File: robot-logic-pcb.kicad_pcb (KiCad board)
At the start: 2 copper layers, 101.6 x 53.3 mm, 21 parts, among them U1 NRF24L01_Breakout

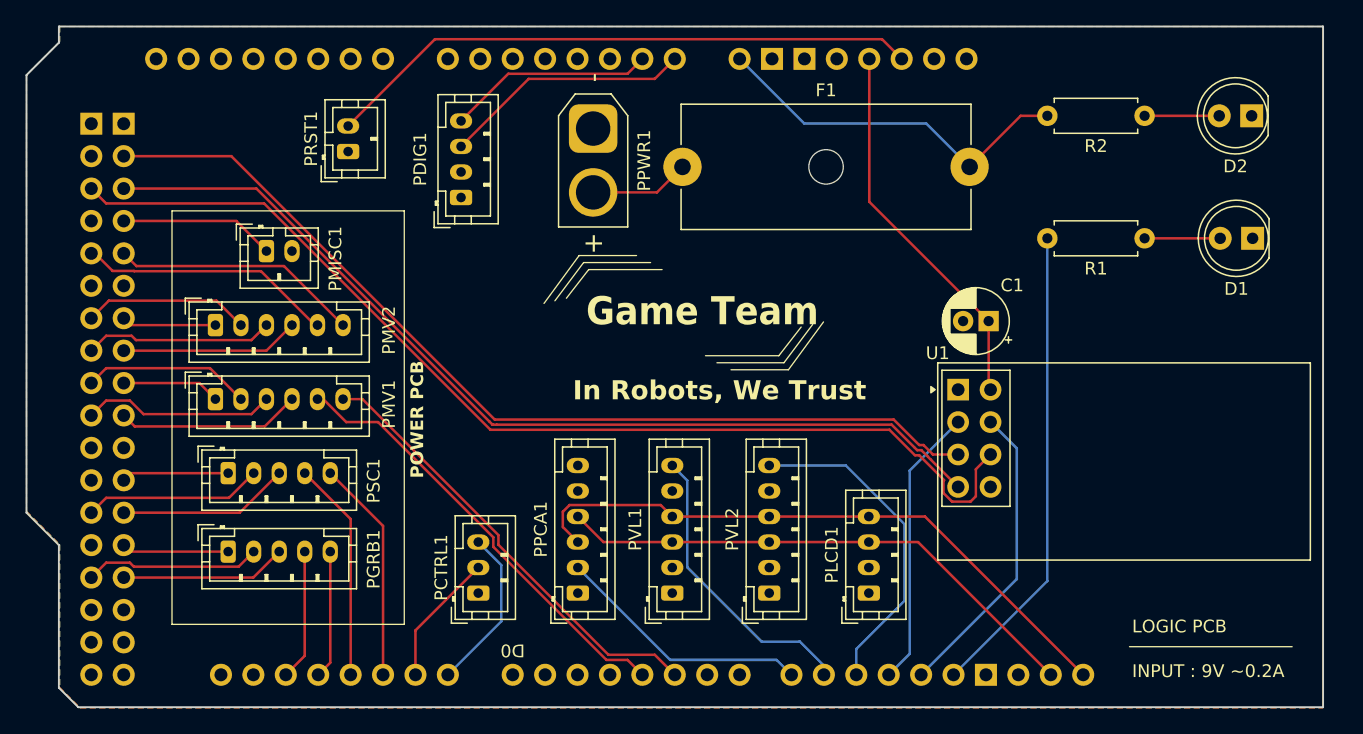
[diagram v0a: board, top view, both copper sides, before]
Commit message: Post regionales Adds ESP32 for steppers and diodes to protect MCUs
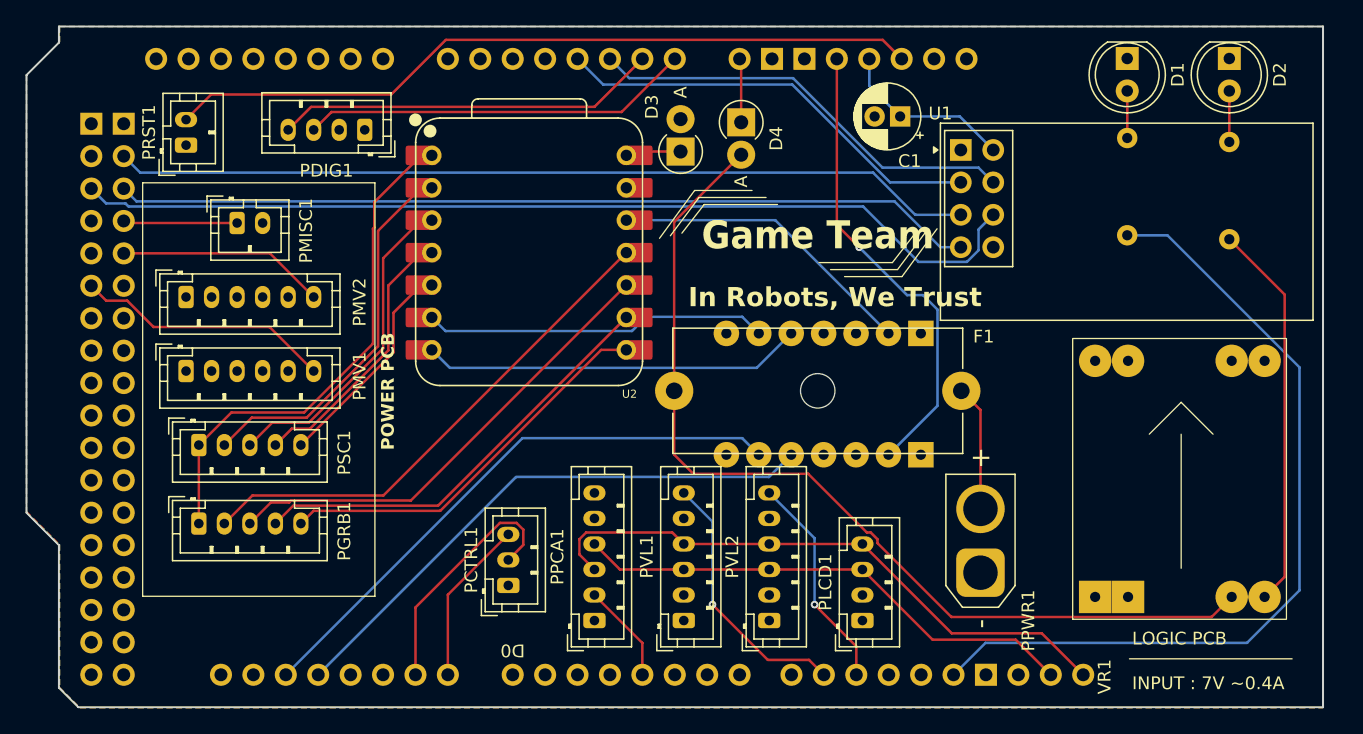
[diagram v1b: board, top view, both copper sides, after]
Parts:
- added D3: 1N4007, Diode_THT:D_DO-41_SOD81_P2.54mm_Vertical_AnodeUp, F.Cu at (118.2, -15.0)
- added D4: 1N4007, Diode_THT:D_DO-41_SOD81_P2.54mm_Vertical_AnodeUp, F.Cu at (123.0, -17.3)
- added U2: XIAO-ESP32-S3-DIP, Project:XIAO-ESP32S3-DIP, F.Cu at (106.4, -7.08)
- added U3: ~, Project:TXB0104-BREAKOUT, B.Cu at (129.5, 3.01)
- added VR1: Voltage Regulator, Project:MP1584EN, F.Cu at (149.0, 21.6)
- R1: moved to B.Cu
- R2: value 220 -> 160; moved to B.Cu
- moved PPWR1 46.2 mm to (141.8, 18.0), turned to 90 degrees
- moved F1 28.0 mm to (140.2, 3.75), turned to 180 degrees
- moved U1 18.8 mm to (140.2, -15.1)
- moved C1 17.5 mm to (135.5, -17.8)
- moved D1 17.2 mm to (153.2, -22.3), turned to -90 degrees
- moved PRST1 12.7 mm to (79.5, -15.5)
- moved PDIG1 9.22 mm to (93.5, -16.7), turned to 180 degrees
- moved R1 7.98 mm to (153.2, -16.1), turned to -90 degrees
- moved R2 6.95 mm to (161.2, -15.8), turned to -90 degrees
- moved D2 4.82 mm to (161.2, -22.3), turned to -90 degrees
- moved PGRB1 3.18 mm to (80.5, 14.2)
- moved PMISC1 3.18 mm to (83.5, -9.40)
- moved PMV1 3.18 mm to (79.5, 2.20)
- moved PMV2 3.18 mm to (79.5, -3.60)
- moved PSC1 3.18 mm to (80.5, 8.00)
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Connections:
- net L298N_R_ENA renamed SBR_R
- A1 pad 5V1: +5V -> ARD_VREF
- A1 pad 5V3: +5V -> unconnected-(A1-5V-Pad5V3)
- A1 pad 5V4: +5V -> unconnected-(A1-5V-Pad5V4)
- A1 pad A2: unconnected-(A1-PadA2) -> /RF_CSN
- A1 pad A3: unconnected-(A1-PadA3) -> /RF_CE
- A1 pad D11: /RF_CE -> unconnected-(A1-PadD11)
- A1 pad D12: /RF_CSN -> unconnected-(A1-PadD12)
- A1 pad D16: SC_RX -> unconnected-(A1-D16/TX2-PadD16)
- A1 pad D17: SC_TX -> unconnected-(A1-D17/RX2-PadD17)
- A1 pad D18: GRB_RX -> ESP_RX_ARD_TX_HV
- A1 pad D19: GRB_TX -> ESP_TX_ARD_RX_HV
- A1 pad D26: GRB_DIR -> unconnected-(A1-PadD26)
- A1 pad D27: GRB_STEP -> unconnected-(A1-PadD27)
- A1 pad D28: GRB_EN -> unconnected-(A1-PadD28)
- A1 pad D30: SC_DIR -> unconnected-(A1-PadD30)
- A1 pad D31: SC_STEP -> unconnected-(A1-PadD31)
- A1 pad D32: SC_EN -> unconnected-(A1-PadD32)
- A1 pad D36: L298N_L_IN1 -> unconnected-(A1-PadD36)
- A1 pad D37: L298N_L_IN2 -> unconnected-(A1-PadD37)
- A1 pad D38: L298N_L_IN4 -> unconnected-(A1-PadD38)
- A1 pad D39: L298N_L_IN3 -> unconnected-(A1-PadD39)
- A1 pad D4: L298N_L_ENB -> PCA9685_EN
- A1 pad D40: L298N_R_IN1 -> unconnected-(A1-PadD40)
- A1 pad D41: L298N_R_IN2 -> unconnected-(A1-PadD41)
- A1 pad D42: L298N_R_IN4 -> unconnected-(A1-PadD42)
- A1 pad D43: L298N_R_IN3 -> unconnected-(A1-PadD43)
- A1 pad D45: unconnected-(A1-PadD45) -> SBR_L
- A1 pad D47: L298N_R_ENB -> unconnected-(A1-PadD47)
- A1 pad D5: L298N_L_ENA -> unconnected-(A1-PadD5)
- A1 pad D8: PCA9685_EN -> unconnected-(A1-PadD8)
- A1 pad VIN: +9V -> Net-(D4-K)
- F1 pad 2: +9V -> +7V
- PGRB1 pad 1: GRB_EN -> STEPPERS_EN
- PMV1 pad 1: L298N_L_IN4 -> unconnected-(PMV1-Pin_1-Pad1)
- PMV1 pad 2: L298N_L_IN3 -> unconnected-(PMV1-Pin_2-Pad2)
- PMV1 pad 3: L298N_L_IN2 -> unconnected-(PMV1-Pin_3-Pad3)
- PMV1 pad 4: L298N_L_IN1 -> unconnected-(PMV1-Pin_4-Pad4)
- PMV1 pad 5: L298N_L_ENB -> unconnected-(PMV1-Pin_5-Pad5)
- PMV1 pad 6: L298N_L_ENA -> SBR_L
- PMV2 pad 1: L298N_R_IN4 -> unconnected-(PMV2-Pin_1-Pad1)
- PMV2 pad 2: L298N_R_IN3 -> unconnected-(PMV2-Pin_2-Pad2)
- PMV2 pad 3: L298N_R_IN2 -> unconnected-(PMV2-Pin_3-Pad3)
- PMV2 pad 4: L298N_R_IN1 -> unconnected-(PMV2-Pin_4-Pad4)
- PMV2 pad 5: L298N_R_ENB -> unconnected-(PMV2-Pin_5-Pad5)
- PSC1 pad 1: SC_EN -> STEPPERS_EN
- R2 pad 2: +9V -> +7V
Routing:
- net +7V: track 0.00 -> 108.5 mm
- net ESP_TX_ARD_RX_HV: track 0.00 -> 45.3 mm
- net ESP_RX_ARD_TX_HV: track 0.00 -> 44.2 mm
- net STEPPERS_EN: track 0.00 -> 39.4 mm
- net ARD_VREF: track 0.00 -> 36.6 mm, vias 0 -> 1
- net L298N_L_ENA: track 35.4 -> 0.00 mm
- net L298N_L_ENB: track 34.8 -> 0.00 mm
- net ESP_RX_ARD_TX_LV: track 0.00 -> 29.9 mm
- net +9V: track 29.3 -> 0.00 mm
- net STATUS_LED: track 37.2 -> 65.1 mm
- net ESP_TX_ARD_RX_LV: track 0.00 -> 27.1 mm
- net GRB_STEP: track 13.8 -> 40.3 mm
- net GRB_DIR: track 13.0 -> 37.2 mm
- net ESP_VREF: track 0.00 -> 24.2 mm
- net GRB_TX: track 10.3 -> 34.2 mm
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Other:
- board text added: "INPUT : 7V ~0.4A"
- board text removed: "INPUT : 9V ~0.2A"
